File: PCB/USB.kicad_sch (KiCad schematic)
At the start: 8 parts, among them J2 Power, J3 I/O, U5 TUSB321

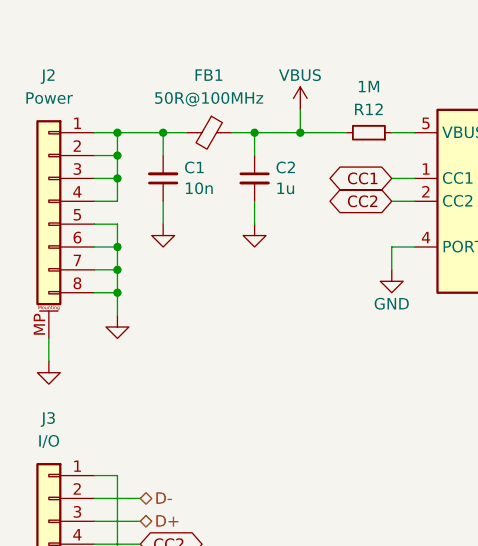
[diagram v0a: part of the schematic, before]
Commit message: 25/07/2023 update
Changed 8 pin JST SH connector to 6 pin. Pushed JST connectors back. Improved 3D model of SSD1351. Minor fix to PER56 footprint.
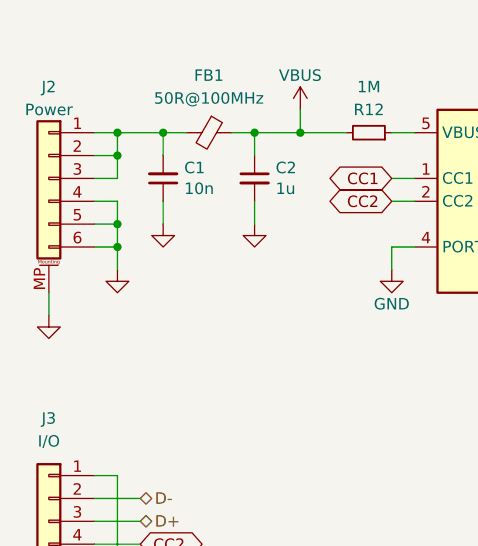
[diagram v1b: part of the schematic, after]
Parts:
- J2: footprint Honeydew:JST_SH_SM08B-SRSS-TB_1x08-1MP_P1.00mm_Horizontal -> Honeydew:JST_SH_SM06B-SRSS-TB_1x06-1MP_P1.00mm_Horizontal; symbol Connector_Generic_MountingPin:Conn_01x08_MountingPin -> Connector_Generic_MountingPin:Conn_01x06_MountingPin; LCSC C160407 -> C160405
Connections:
- net GND: now also J2.4 (Pin_4); no longer J2.7 (Pin_7), J2.8 (Pin_8)
- net at C1.2, FB1.2, J2.1 (Pin_1)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: no longer J2.4 (Pin_4)

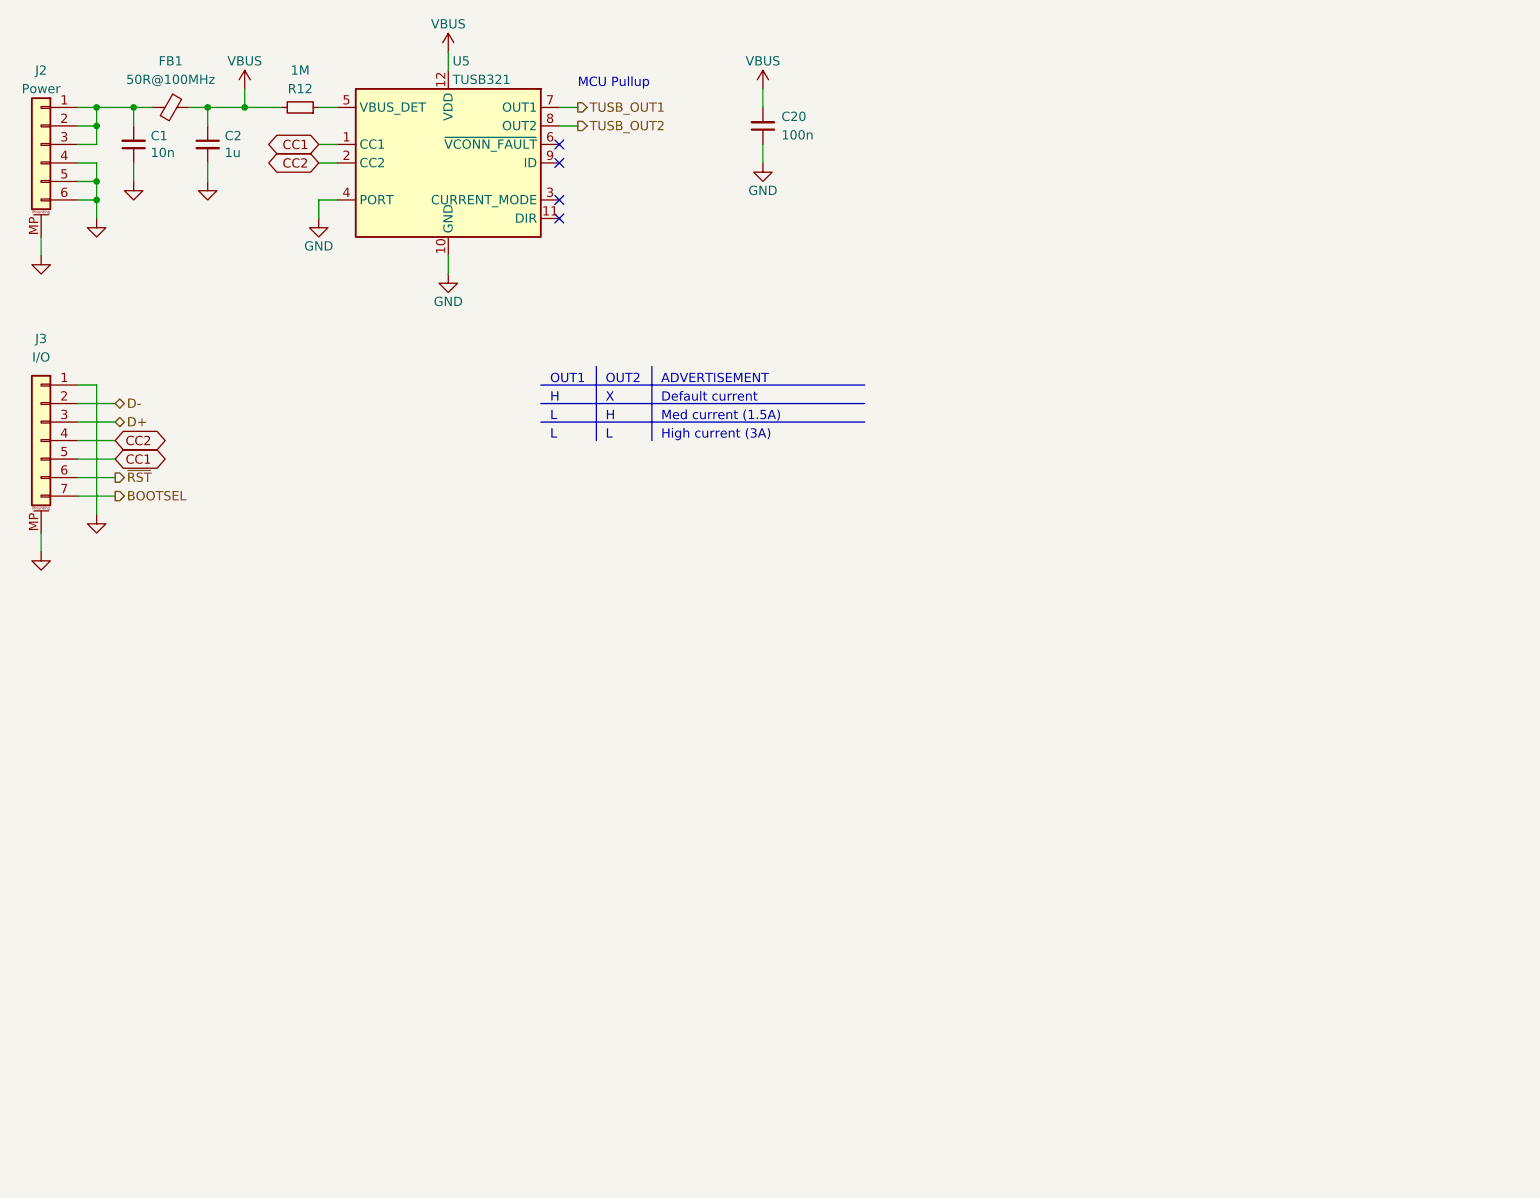
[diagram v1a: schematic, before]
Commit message: 28/07/2023 update
Removed center ring encoder, cirque trackpad and PMW3360 support. Added VIK header and hole in the center of the PCB for the Kiwano. Changed JST connectors back to 20 pin FFC. Total rearrangement of parts in keyboard center. Stitched ground planes together. Added USB module to board rather than have it be separate.
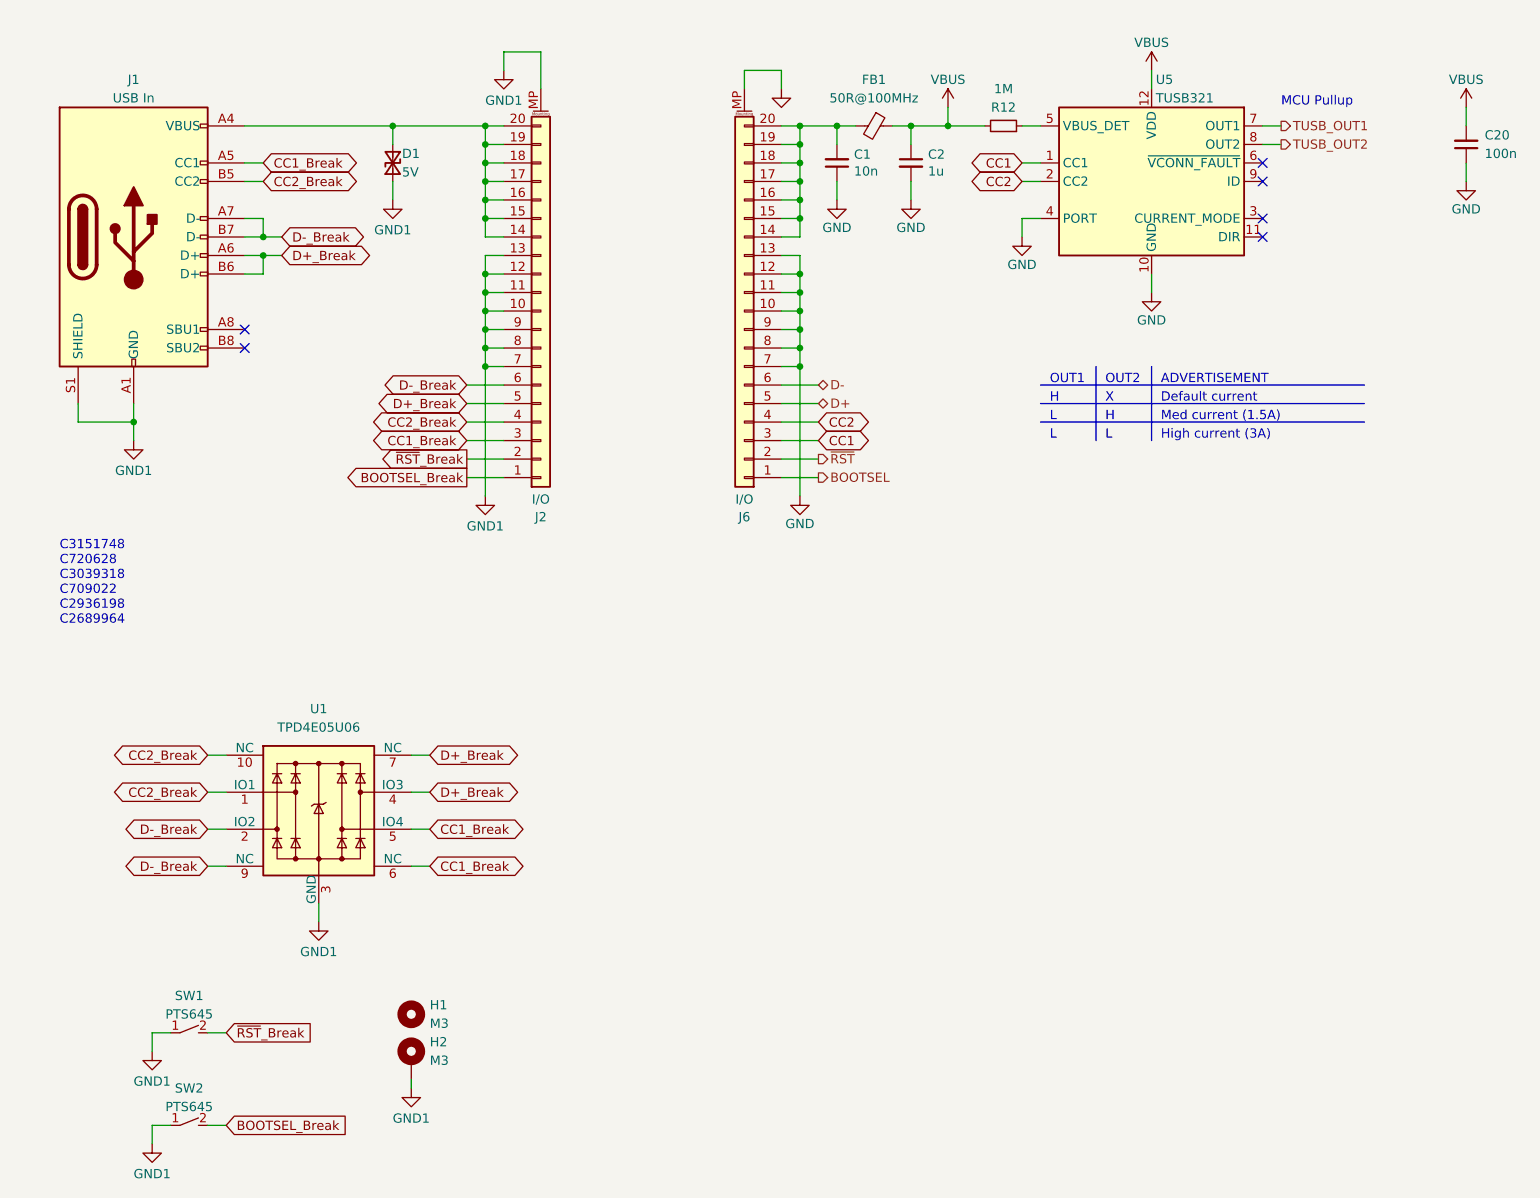
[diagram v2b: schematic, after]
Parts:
- removed J2: Power, Honeydew:JST_SH_SM06B-SRSS-TB_1x06-1MP_P1.00mm_Horizontal, symbol Connector_Generic_MountingPin:Conn_01x06_MountingPin
- removed J3: I/O, Honeydew:JST_SH_SM07B-SRSS-TB_1x07-1MP_P1.00mm_Horizontal, symbol Connector_Generic_MountingPin:Conn_01x07_MountingPin
- added D1: 5V, Diode_SMD:D_SOD-523, symbol Galia:D_TVS_Small
- added H1: M3, Honeydew:MountingHole_3.2mm_M3_Pad, symbol Mechanical:MountingHole
- added H2: M3, Honeydew:MountingHole_3.2mm_M3_Pad, symbol Mechanical:MountingHole_Pad
- added J1: USB In, Honeydew:CON-USB4120-03-C-REVA, symbol Connector:USB_C_Receptacle_USB2.0
- added J2, J6: I/O, Honeydew:HRS_FH34SRJ-20S-0.5SH(50), symbol Connector_Generic_MountingPin:Conn_01x20_MountingPin
- added SW1, SW2: PTS645, Honeydew:SW_SPST_PTS645, symbol Cantaloupe:SW_SPST_Small
- added U1: TPD4E05U06, Honeydew:USON-10_2.5x1.0mm_P0.5mm, symbol Galia:TPD4E05U06
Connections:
- net BOOTSEL: now also J6.1 (Pin_1)
- net CC1: now also J6.3 (Pin_3)
- net CC2: now also J6.4 (Pin_4)
- net D+: now also J6.5 (Pin_5)
- net D-: now also J6.6 (Pin_6)
- net GND: now also D1.2 (A), H2.1, J1.A1 (GND), J1.A12 (GND), J1.B1 (GND), J1.B12 (GND), J1.S1 (SHIELD), J2.10 (Pin_10), J2.11 (Pin_11), J2.12 (Pin_12), J2.13 (Pin_13), J2.7 (Pin_7), J2.8 (Pin_8), J2.9 (Pin_9), J2.MP (MountPin), J6.10 (Pin_10), J6.11 (Pin_11), J6.12 (Pin_12), J6.13 (Pin_13), J6.7 (Pin_7), J6.8 (Pin_8), J6.9 (Pin_9), J6.MP (MountPin), SW1.1 (A), SW2.1 (A), U1.3 (GND), U1.8 (GND)
- net ~{RST}: now also J6.2 (Pin_2)
- net at C1.2, FB1.2: now also J6.14 (Pin_14), J6.15 (Pin_15), J6.16 (Pin_16), J6.17 (Pin_17), J6.18 (Pin_18), J6.19 (Pin_19), J6.20 (Pin_20)
- new net: D1.1 (K), J1.A4 (VBUS), J1.A9 (VBUS), J1.B4 (VBUS), J1.B9 (VBUS), J2.14 (Pin_14), J2.15 (Pin_15), J2.16 (Pin_16), J2.17 (Pin_17), J2.18 (Pin_18), J2.19 (Pin_19), J2.20 (Pin_20)
- new net BOOTSEL_Break: J2.1 (Pin_1), SW2.2 (B)
- new net CC1_Break: J1.A5 (CC1), J2.3 (Pin_3), U1.5 (IO4), U1.6 (NC)
- new net CC2_Break: J1.B5 (CC2), J2.4 (Pin_4), U1.1 (IO1), U1.10 (NC)
- new net D+_Break: J1.A6 (D+), J1.B6 (D+), J2.5 (Pin_5), U1.4 (IO3), U1.7 (NC)
- new net D-_Break: J1.A7 (D-), J1.B7 (D-), J2.6 (Pin_6), U1.2 (IO2), U1.9 (NC)
- new net ~{RST}_Break: J2.2 (Pin_2), SW1.2 (B)
- no-connect marks 4 -> 6
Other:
- note added: "C3151748 C720628 C3039318 C709022 C2936198 C2689964"
- company: (none) -> Created by Ariamelon (https://github.com/Ariamelon/Honeydew/)
- title: (none) -> Honeydew unified split ergonomic keyboard
- moved on the sheet: C1, C2, C20, FB1, R12, U5

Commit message: 30/07/2023 update
Added VIK keyboard certification card. Added USB connector back to PCB, but left the two buttons on a separate daughterboard. Modified case to accommodate large VIK module.
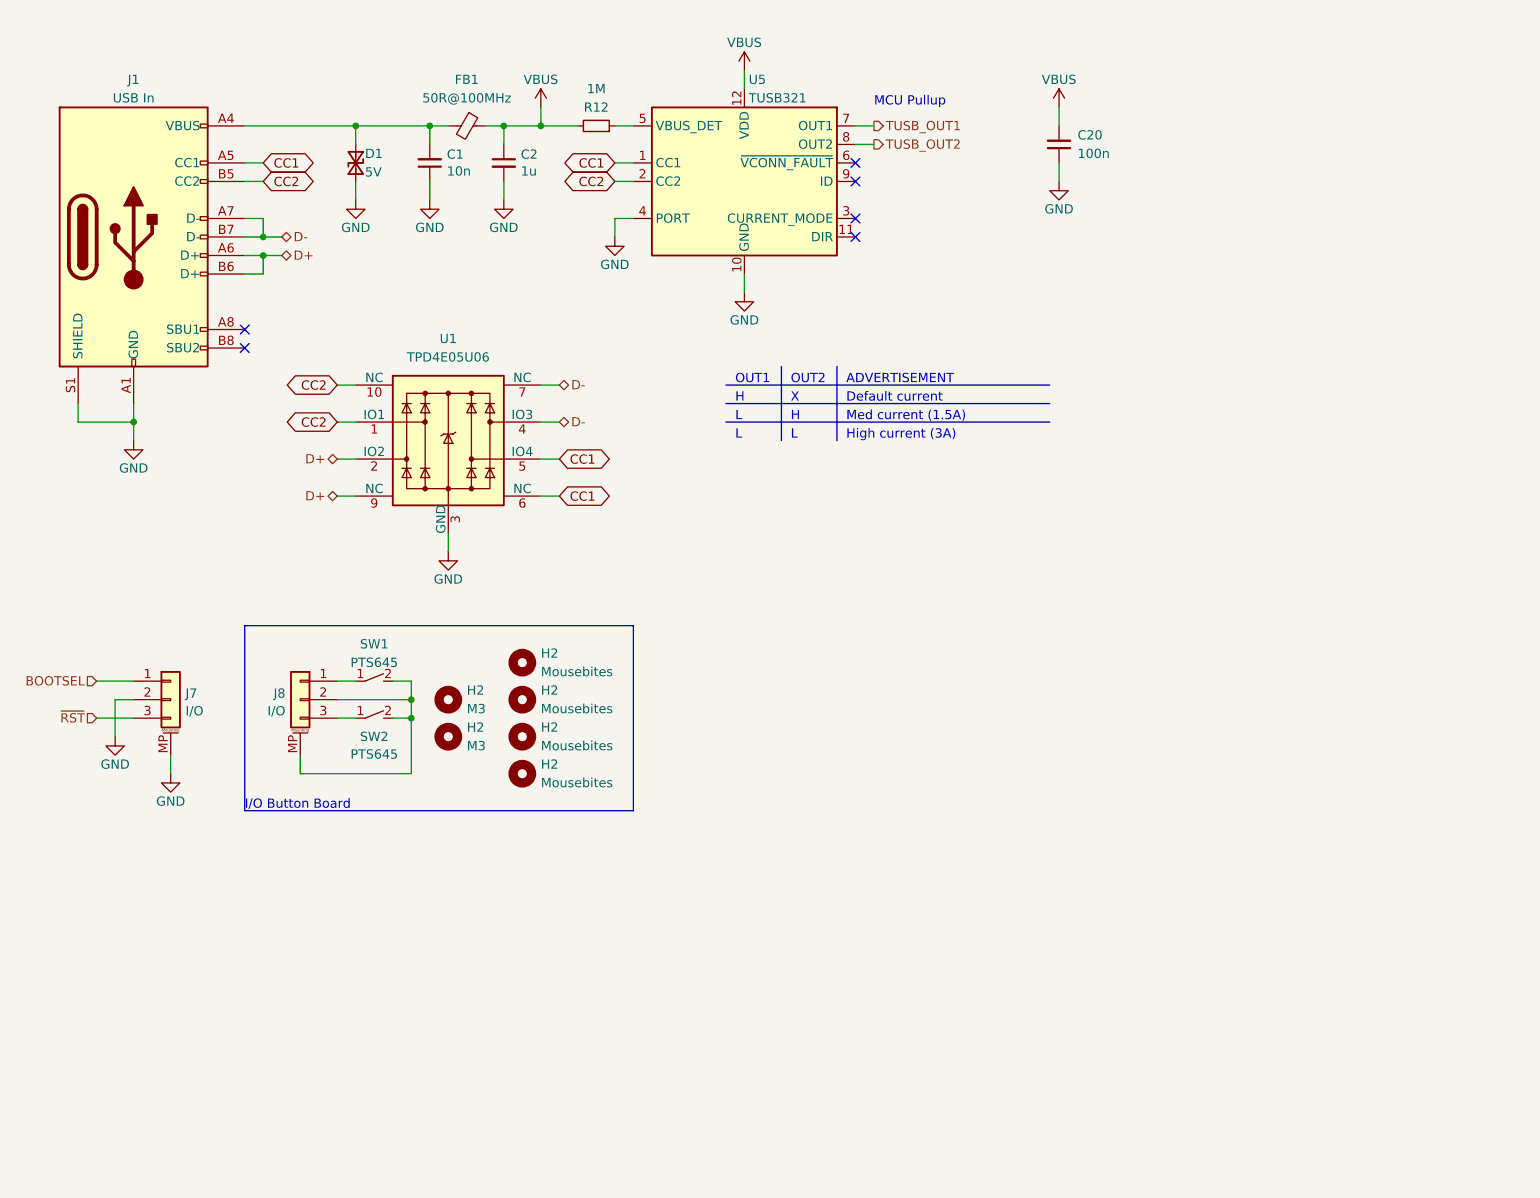
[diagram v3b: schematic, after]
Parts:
- removed H1: M3, Honeydew:MountingHole_3.2mm_M3_Pad, symbol Mechanical:MountingHole
- removed H2: M3, Honeydew:MountingHole_3.2mm_M3_Pad, symbol Mechanical:MountingHole_Pad
- removed J2, J6: I/O, Honeydew:HRS_FH34SRJ-20S-0.5SH(50), symbol Connector_Generic_MountingPin:Conn_01x20_MountingPin
- added H2 (x2): M3, Honeydew:MountingHole_3.2mm_M3_Pad, symbol Mechanical:MountingHole
- added H2 (x4): Mousebites, Honeydew:Mousebites, symbol Mechanical:MountingHole
- added J7, J8: I/O, Honeydew:JST_SH_SM03B-SRSS-TB_1x03-1MP_P1.00mm_Horizontal, symbol Connector_Generic_MountingPin:Conn_01x03_MountingPin
- J1: footprint Honeydew:CON-USB4120-03-C-REVA -> Honeydew:HRO-TYPE-C-31-M-13x; LCSC C709022 -> C3019720
- SW1, SW2: LCSC C285487 -> C285466
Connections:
- net CC1_Break is gone; now on net CC1: J1.A5 (CC1), U1.5 (IO4), U1.6 (NC)
- net CC2_Break is gone; now on net CC2: J1.B5 (CC2), U1.1 (IO1), U1.10 (NC)
- net ~{RST}_Break is gone; now on an unnamed net: SW1.2 (B)
- net BOOTSEL: now also J7.1 (Pin_1)
- net D+: now also J1.A6 (D+), J1.B6 (D+), U1.2 (IO2), U1.9 (NC)
- net D-: now also J1.A7 (D-), J1.B7 (D-), U1.4 (IO3), U1.7 (NC)
- net GND: now also J7.2 (Pin_2), J7.MP (MountPin); no longer SW1.1 (A), SW2.1 (A)
- net ~{RST}: now also J7.3 (Pin_3)
- net at C1.2, FB1.2: now also D1.1 (K), J1.A4 (VBUS), J1.A9 (VBUS), J1.B4 (VBUS), J1.B9 (VBUS)
- net BOOTSEL_Break: no longer names the net of SW2.2 (B)
- net BOOTSEL_Break: now also J8.2 (Pin_2), J8.MP (MountPin)
- removed net D+_Break: J1.A6 (D+), J1.B6 (D+), U1.4 (IO3), U1.7 (NC)
- removed net D-_Break: J1.A7 (D-), J1.B7 (D-), U1.2 (IO2), U1.9 (NC)
- new net: J8.1 (Pin_1), SW1.1 (A)
- new net: J8.3 (Pin_3), SW2.1 (A)
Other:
- note added: "I/O Button Board"
- note removed: "C3151748 C720628 C3039318 C709022 C2936198 C2689964"
- moved on the sheet: C1, C2, C20, D1, FB1, R12, SW1, SW2, U1, U5

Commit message: Updated production files.
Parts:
- J7, J8: LCSC C160389 -> C160403
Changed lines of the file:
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@@
       (effects (font (size 1.27 1.27)) hide)
     )
-    (property "LCSC" "C160389" (at 38.1 109.22 0)
+    (property "LCSC" "C160403" (at 38.1 109.22 0)
       (effects (font (size 1.27 1.27)) hide)
     )
@@
       (effects (font (size 1.27 1.27)) hide)
     )
-    (property "LCSC" "C160389" (at 55.88 109.22 0)
+    (property "LCSC" "C160403" (at 55.88 109.22 0)
       (effects (font (size 1.27 1.27)) hide)
     )

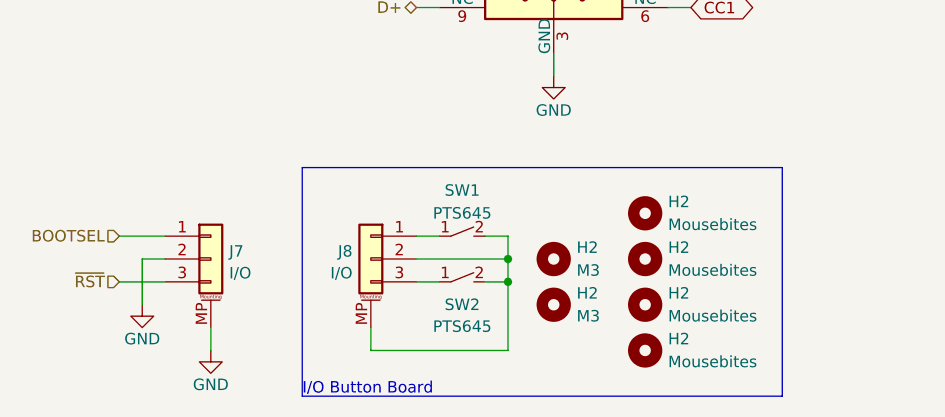
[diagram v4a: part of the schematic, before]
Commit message: 31/07/2023 update
Removed button daughterboard. Reduced size of case and gaskets and added locating features. Added o-ring mounting for the PCB to the bottom case. Added fittings BOM.
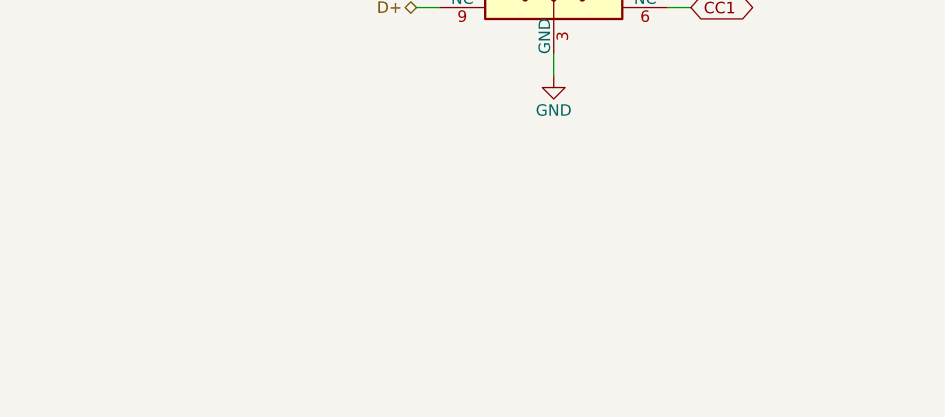
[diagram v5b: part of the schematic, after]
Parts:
- removed H2 (x2): M3, Honeydew:MountingHole_3.2mm_M3_Pad, symbol Mechanical:MountingHole
- removed H2 (x4): Mousebites, Honeydew:Mousebites, symbol Mechanical:MountingHole
- removed J7, J8: I/O, Honeydew:JST_SH_SM03B-SRSS-TB_1x03-1MP_P1.00mm_Horizontal, symbol Connector_Generic_MountingPin:Conn_01x03_MountingPin
- removed SW1, SW2: PTS645, Honeydew:SW_SPST_PTS645, symbol Cantaloupe:SW_SPST_Small
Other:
- note removed: "I/O Button Board"
